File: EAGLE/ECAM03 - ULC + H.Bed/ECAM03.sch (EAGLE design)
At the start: 45 parts, among them J1 MODULAR TOOL, J2 FAN1, J3 FAN2, J4 FAN3, J5 S4B-PH-SM4, J6 SSR, J7 RINGLIGHT, J8 FTDI, J9 SPI, Q2 16MHz, U1 SP3485, U2 ATMEGA238, U3 MCP4725, U4 MAX31855, U5 NTR4003NT3G, U6 NOR(74LVC), U8 AP3032

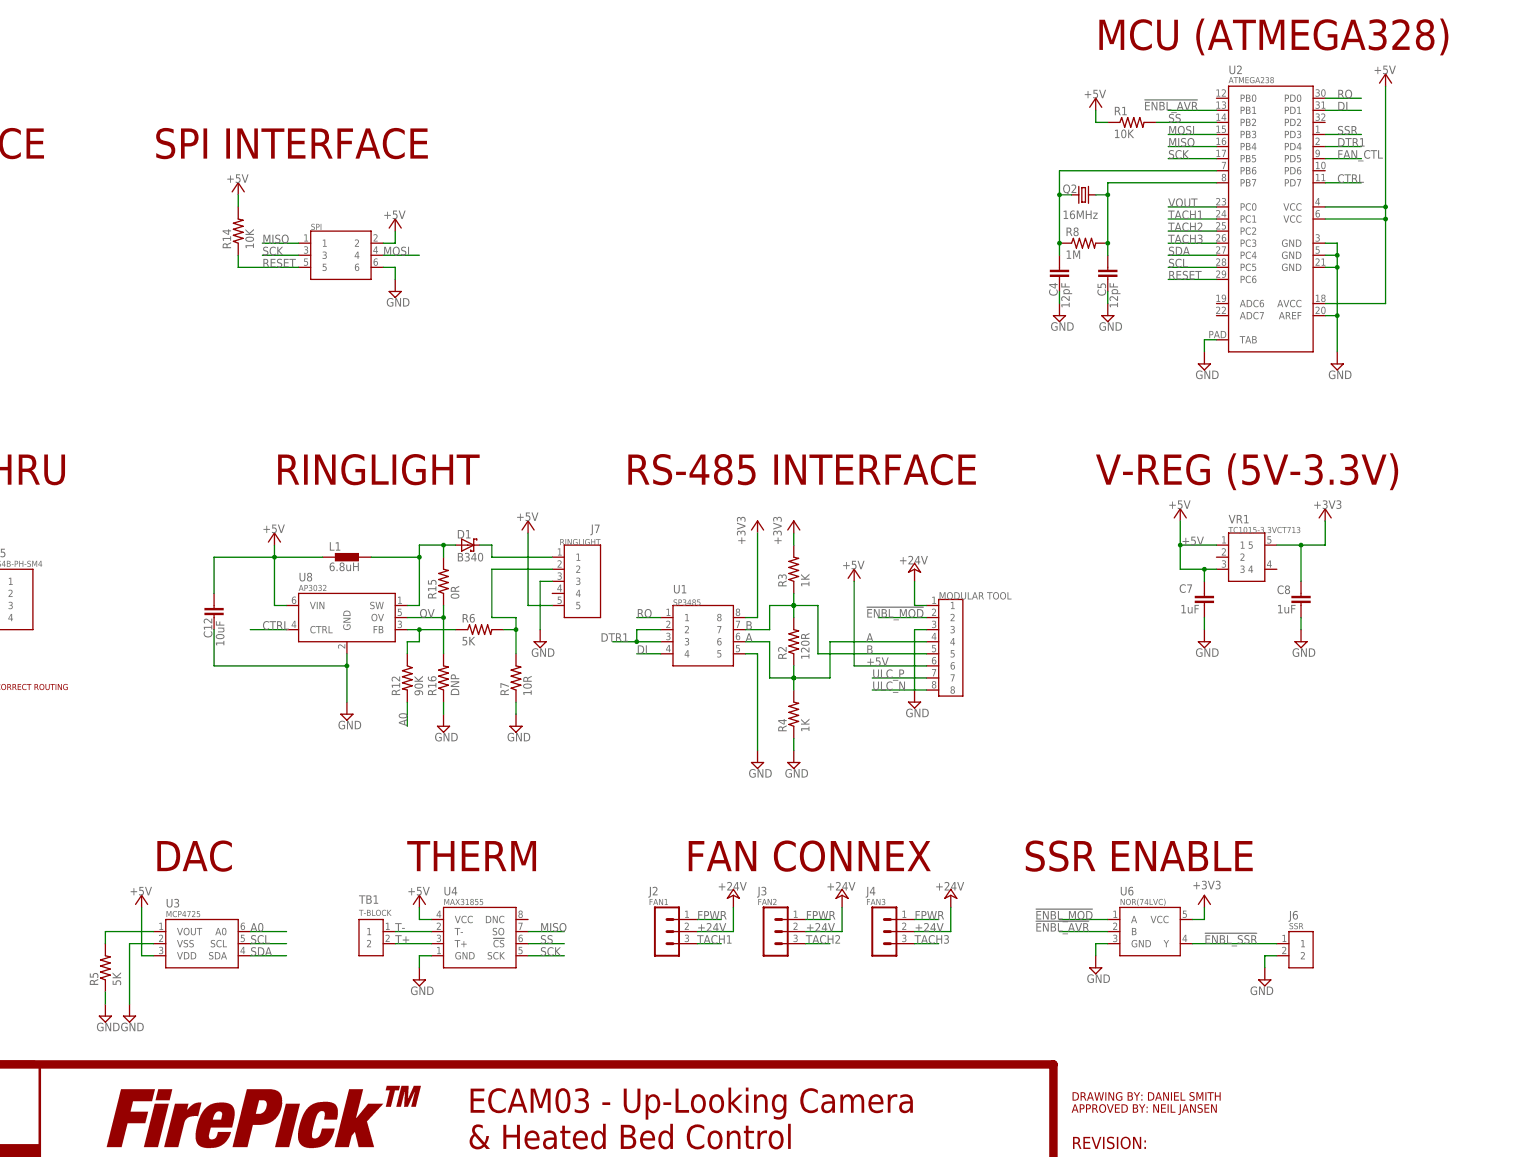
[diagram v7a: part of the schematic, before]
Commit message: Re-jiggered switching power for LED controller, rerouted and whatnot.  Added trace for WS2812B.  Swapped DAC wire (A0 was going to the LED driver instead of analog out).  Generated GERBERs for Rev--.
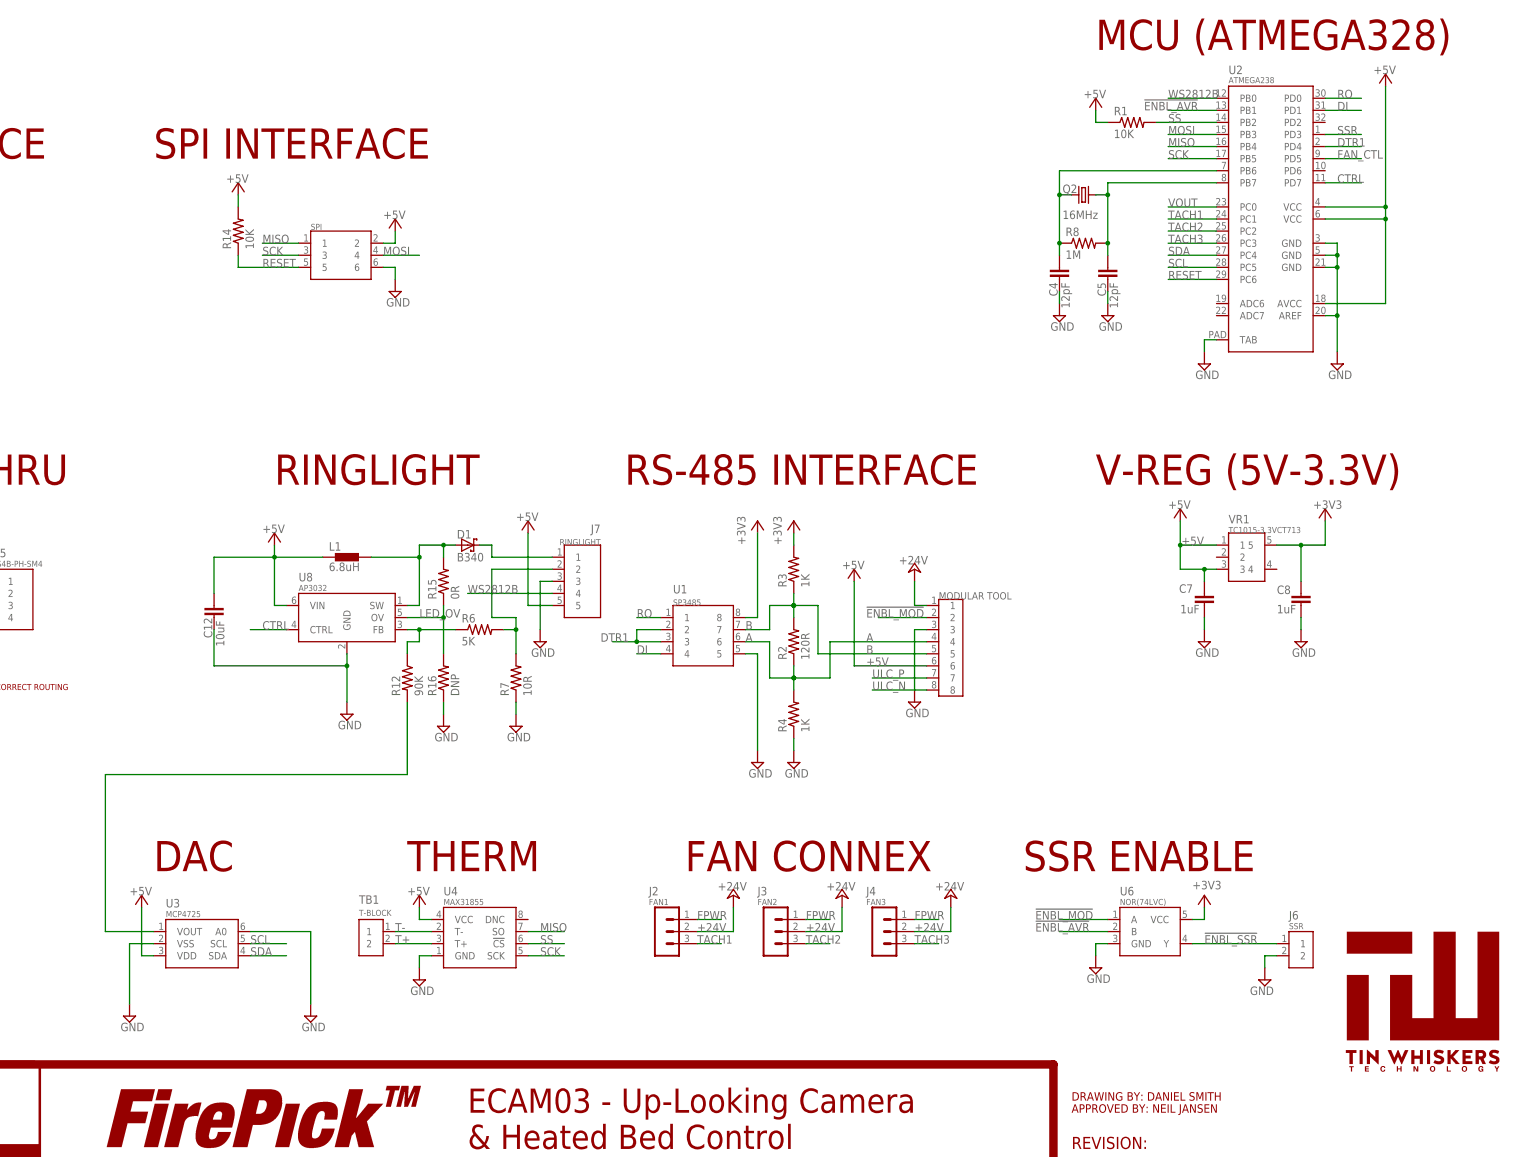
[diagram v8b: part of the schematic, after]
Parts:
- removed R5: 5K, TinWhiskers:CPL-RES-0603-5K-0.1W
- added U$1: TIN-WHISKERSTSTOP, !tin-whiskers-logo:TIN-WHISKERSTSTOP
- R7: device TinWhiskers:CPL-RES-0603-10.0-0.1W -> TinWhiskers:CPL-RES-1206-10-0.25W1206
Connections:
- net N$1 renamed LED_+
- net N$2 renamed LED_SW
- net N$4 renamed LED_FB
- net N$6 renamed LED_-
- net OV renamed LED_OV
- removed net A0: R12.2, U3.A0
- new net WS2812B: J7.4, U2.PB0
- net GND: now also U3.A0; no longer R5.1
- net N$5: now also R12.2; no longer R5.2
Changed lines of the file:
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@@
 <?xml version="1.0" encoding="utf-8"?>
 <!DOCTYPE eagle SYSTEM "eagle.dtd">
-<eagle version="7.4.0">
+<eagle version="7.3.0">
 <drawing>
 <settings>
@@
 <part name="P+5" library="supply1" deviceset="+5V" device=""/>
 <part name="SUPPLY4" library="TinWhiskers" deviceset="GND" device=""/>
-<part name="R5" library="TinWhiskers" deviceset="CPL-RES-0603-5K-0.1W" device="" value="5K"/>
-<part name="SUPPLY5" library="TinWhiskers" deviceset="GND" device=""/>
 <part name="U4" library="TinWhiskers" deviceset="CPL-THRM-MAX31855" device="" value="MAX31855"/>
 <part name="SUPPLY6" library="TinWhiskers" deviceset="GND" device=""/>
@@
 <part name="SUPPLY13" library="TinWhiskers" deviceset="GND" device=""/>
 <part name="R6" library="TinWhiskers" deviceset="CPL-RES-0603-5K-0.1W" device="" value="5K"/>
-<part name="R7" library="TinWhiskers" deviceset="CPL-RES-0603-10.0-0.1W" device="" value="10R"/>
+<part name="R7" library="TinWhiskers" deviceset="CPL-RES-1206-10-0.25W" device="1206" value="10R"/>
 <part name="R12" library="TinWhiskers" deviceset="CPL-RES-0603-90K-0.1W" device="" value="90K"/>
 <part name="SUPPLY16" library="TinWhiskers" deviceset="GND" device=""/>
@@
 <part name="P+16" library="supply1" deviceset="+5V" device=""/>
 <part name="SUPPLY18" library="TinWhiskers" deviceset="GND" device=""/>
+<part name="U$1" library="!tin-whiskers-logo" deviceset="TIN-WHISKERS" device="TSTOP"/>
+<part name="SUPPLY5" library="TinWhiskers" deviceset="GND" device=""/>
 </parts>
 <sheets>
@@
 <attribute name="VALUE" x="92.075" y="34.925" size="1.778" layer="96"/>
 </instance>
-<instance part="R5" gate="G$1" x="88.9" y="48.26" rot="R90"/>
-<instance part="SUPPLY5" gate="GND" x="88.9" y="38.1" smashed="yes">
-<attribute name="VALUE" x="86.995" y="34.925" size="1.778" layer="96"/>
-</instance>
 <instance part="U4" gate="G$1" x="167.64" y="55.88"/>
 <instance part="SUPPLY6" gate="GND" x="154.94" y="45.72" smashed="yes">
@@
 <instance part="SUPPLY18" gate="GND" x="149.86" y="190.5" smashed="yes">
 <attribute name="VALUE" x="147.955" y="187.325" size="1.778" layer="96"/>
+</instance>
+<instance part="U$1" gate="G$1" x="347.98" y="25.4"/>
+<instance part="SUPPLY5" gate="GND" x="132.08" y="38.1" smashed="yes">
+<attribute name="VALUE" x="130.175" y="34.925" size="1.778" layer="96"/>
 </instance>
 </instances>
@@
 </segment>
 <segment>
-<pinref part="SUPPLY5" gate="GND" pin="GND"/>
-<pinref part="R5" gate="G$1" pin="1"/>
-<wire x1="88.9" y1="40.64" x2="88.9" y2="43.18" width="0.1524" layer="91"/>
-</segment>
-<segment>
 <pinref part="U4" gate="G$1" pin="GND"/>
 <wire x1="157.48" y1="50.8" x2="154.94" y2="50.8" width="0.1524" layer="91"/>
@@
 <wire x1="149.86" y1="195.58" x2="149.86" y2="193.04" width="0.1524" layer="91"/>
 <pinref part="SUPPLY18" gate="GND" pin="GND"/>
+</segment>
+<segment>
+<pinref part="U3" gate="G$1" pin="A0"/>
+<pinref part="SUPPLY5" gate="GND" pin="GND"/>
+<wire x1="119.38" y1="55.88" x2="132.08" y2="55.88" width="0.1524" layer="91"/>
+<wire x1="132.08" y1="55.88" x2="132.08" y2="40.64" width="0.1524" layer="91"/>
 </segment>
 </net>
@@
 </segment>
 </net>
-<net name="N$2" class="0">
+<net name="LED_SW" class="0">
 <segment>
 <pinref part="L1" gate="G$1" pin="2"/>
@@
 </segment>
 </net>
-<net name="OV" class="0">
+<net name="LED_OV" class="0">
 <segment>
 <pinref part="R16" gate="R$1" pin="2"/>
@@
 </segment>
 </net>
-<net name="N$1" class="0">
+<net name="LED_+" class="0">
 <segment>
 <pinref part="D1" gate="G$1" pin="C"/>
@@
 <pinref part="U3" gate="G$1" pin="VOUT"/>
 <wire x1="99.06" y1="55.88" x2="88.9" y2="55.88" width="0.1524" layer="91"/>
-<pinref part="R5" gate="G$1" pin="2"/>
-<wire x1="88.9" y1="53.34" x2="88.9" y2="55.88" width="0.1524" layer="91"/>
-</segment>
-</net>
-<net name="A0" class="0">
-<segment>
-<pinref part="U3" gate="G$1" pin="A0"/>
-<wire x1="119.38" y1="55.88" x2="127" y2="55.88" width="0.1524" layer="91"/>
-<label x="119.38" y="55.88" size="1.778" layer="95"/>
-</segment>
-<segment>
 <pinref part="R12" gate="G$1" pin="2"/>
-<wire x1="152.4" y1="99.06" x2="152.4" y2="104.14" width="0.1524" layer="91"/>
-<label x="152.4" y="99.06" size="1.778" layer="95" ratio="10" rot="R90"/>
+<wire x1="152.4" y1="104.14" x2="152.4" y2="88.9" width="0.1524" layer="91"/>
+<wire x1="152.4" y1="88.9" x2="88.9" y2="88.9" width="0.1524" layer="91"/>
+<wire x1="88.9" y1="88.9" x2="88.9" y2="55.88" width="0.1524" layer="91"/>
 </segment>
 </net>
@@
 </segment>
 </net>
-<net name="N$4" class="0">
+<net name="LED_FB" class="0">
 <segment>
 <pinref part="R12" gate="G$1" pin="1"/>
@@
 </segment>
 </net>
-<net name="N$6" class="0">
+<net name="LED_-" class="0">
 <segment>
 <pinref part="R7" gate="G$1" pin="2"/>
@@
 </segment>
 </net>
+<net name="WS2812B" class="0">
+<segment>
+<pinref part="U2" gate="G$1" pin="PB0"/>
+<wire x1="322.58" y1="231.14" x2="312.42" y2="231.14" width="0.1524" layer="91"/>
+<label x="312.42" y="231.14" size="1.778" layer="95"/>
+</segment>
+<segment>
+<pinref part="J7" gate="G$1" pin="4"/>
+<wire x1="182.88" y1="127" x2="165.1" y2="127" width="0.1524" layer="91"/>
+<label x="165.1" y="127" size="1.778" layer="95"/>
+</segment>
+</net>
